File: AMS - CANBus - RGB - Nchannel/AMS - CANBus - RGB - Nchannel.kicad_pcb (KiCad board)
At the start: 2 copper layers, 72.9 x 71.1 mm, 59 parts, among them J1 Power_And_CAN, J2 Screw_Terminal_01x05, J3 TTL_Programmer, J4 ICSP, J5 Conn_01x02, Q1 IRF9Z34NPBF, Q10 2N7002, Q2 2N7002, Q3 IRF9Z34NPBF, Q4 2N7002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

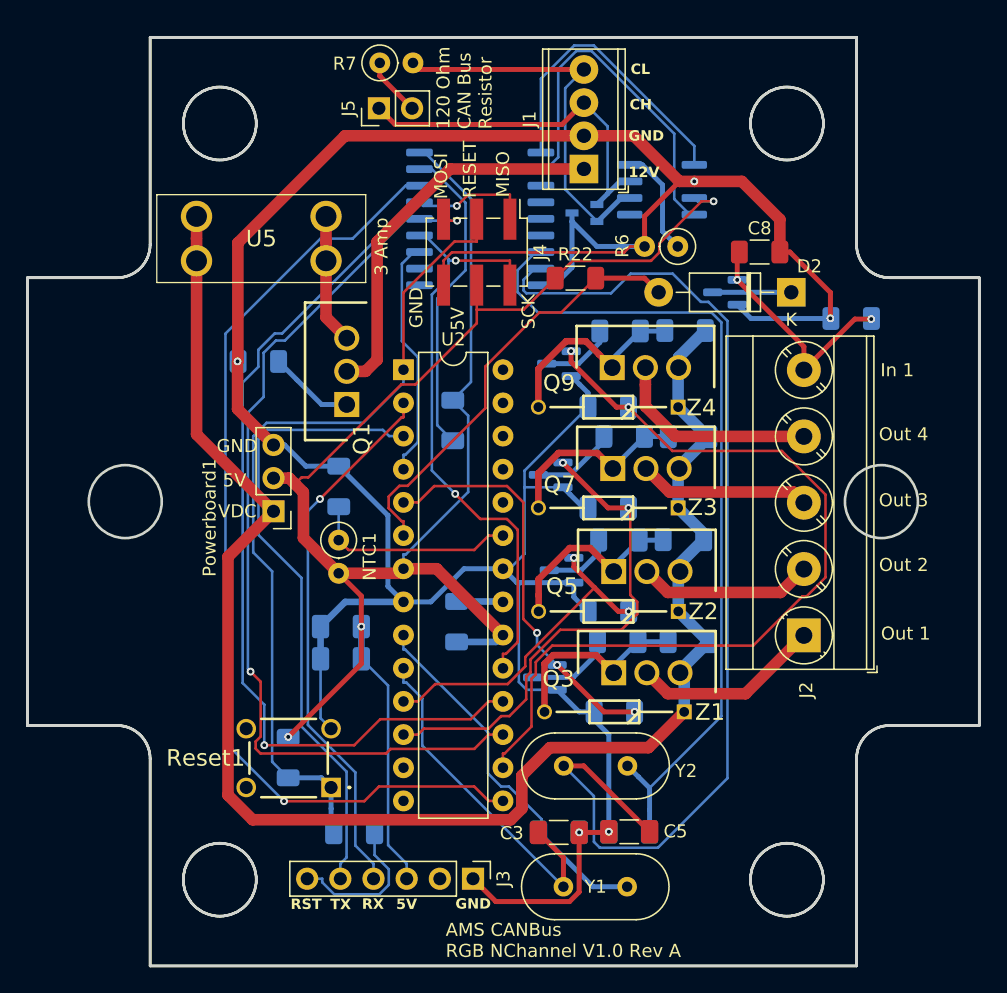
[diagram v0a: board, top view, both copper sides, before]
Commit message: clean up to avoid serpac case mounting bosses.
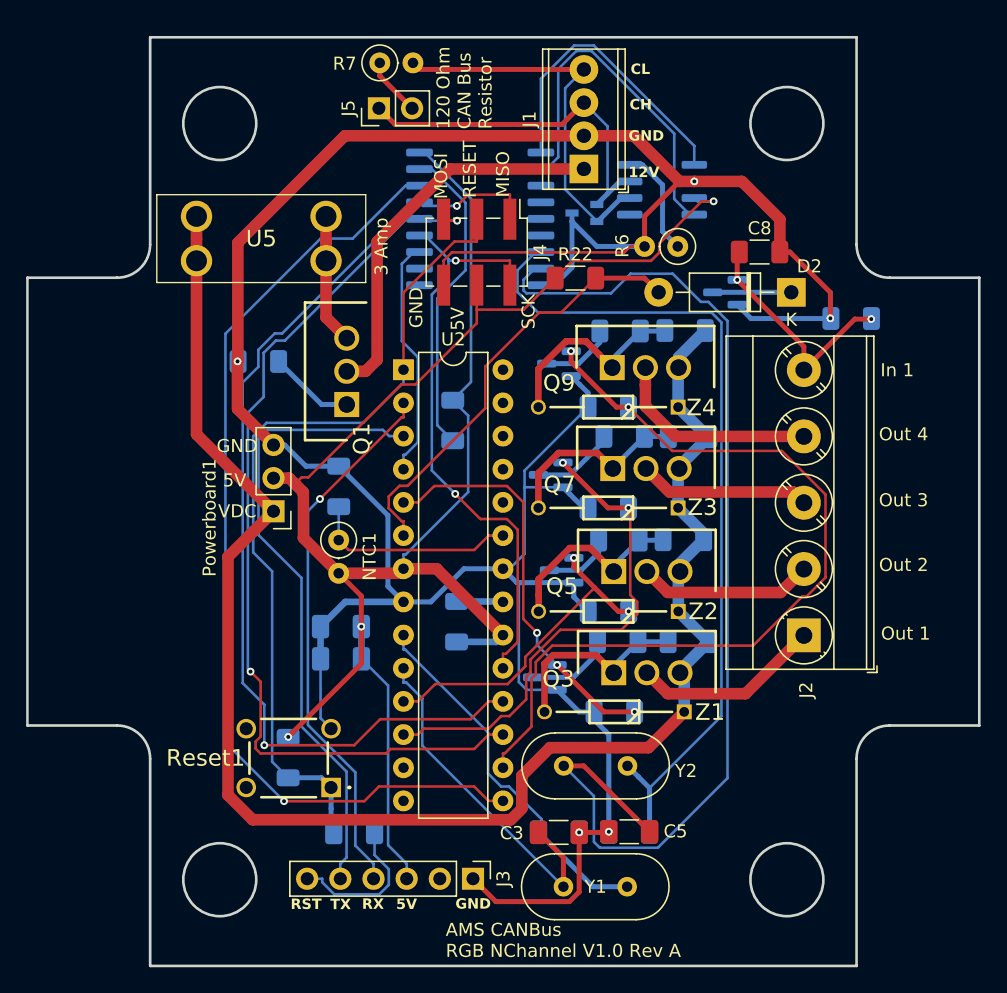
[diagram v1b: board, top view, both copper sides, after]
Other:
- outline, holes or cut-outs redrawn

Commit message: routing and stuff are fixed along with the addition of the I2c bus being pulled out.
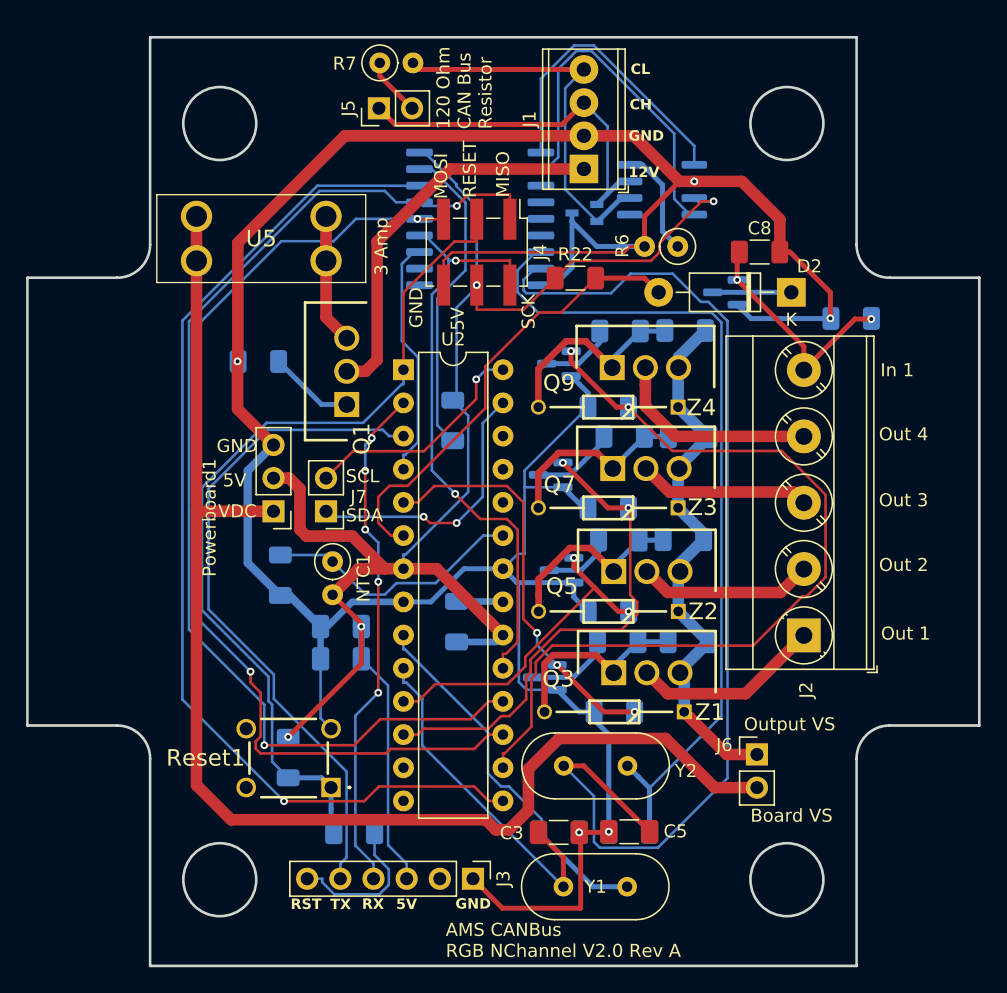
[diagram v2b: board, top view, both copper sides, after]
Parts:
- added J6: Conn_01x02, Connector_PinHeader_2.54mm:PinHeader_1x02_P2.54mm_Vertical, F.Cu at (168.0, 111.2)
- added J7: Conn_01x02, Connector_PinHeader_2.54mm:PinHeader_1x02_P2.54mm_Vertical, F.Cu at (135.0, 92.6)
- moved R3 8.14 mm to (131.5, 97.5), turned to 90 degrees
- moved NTC1 1.71 mm to (135.5, 96.5)
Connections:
- Q3 pad 3: +VDC -> /Output12v/VS
- Q5 pad 3: +VDC -> /Output12v/VS
- Q7 pad 3: +VDC -> /Output12v/VS
- Q9 pad 3: +VDC -> /Output12v/VS
- R12 pad 1: +VDC -> /Output12v/VS
- R15 pad 1: +VDC -> /Output12v/VS
- R18 pad 1: +VDC -> /Output12v/VS
- R9 pad 1: +VDC -> /Output12v/VS
- U2 pad 27: /BareMinAtmel328P/PC4-A4-SDA -> SDA
- U2 pad 28: /BareMinAtmel328P/PC5-A5-SCL -> SCL
- Z1 pad 1: +VDC -> /Output12v/VS
- Z2 pad 1: +VDC -> /Output12v/VS
- Z3 pad 1: +VDC -> /Output12v/VS
- Z4 pad 1: +VDC -> /Output12v/VS
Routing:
- net /Output12v/VS: track 0.00 -> 41.4 mm
- net +VDC: track 125.0 -> 100.1 mm
- net SDA: track 0.00 -> 20.4 mm, vias 0 -> 2
- net SCL: track 0.00 -> 17.9 mm, vias 0 -> 1
- net +5V: track 147.0 -> 129.8 mm, vias 3 -> 4
- net /BareMinAtmel328P/PB4-D12-MISO: track 77.0 -> 85.9 mm
- net /BareMinAtmel328P/PB3-D11-MOSI: track 70.9 -> 76.8 mm
- net /BareMinAtmel328P/PB1-D9: track 74.9 -> 80.2 mm
- net /BareMinAtmel328P/PC0-A0: track 15.9 -> 20.2 mm
- net /BareMinAtmel328P/RESET: track 64.8 -> 68.1 mm
- net /BareMinAtmel328P/PD1-TX: track 48.3 -> 51.5 mm
- net /BareMinAtmel328P/PD0-RX: track 41.6 -> 39.4 mm, vias 1 -> 5
- net /BareMinAtmel328P/PD4-D4: track 33.5 -> 35.1 mm
- net GND: track 233.9 -> 235.0 mm
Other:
- board text added: "AMS CANBus RGB NChannel V2.0 Rev A"
- board text added: "Board VS"
- board text added: "Output VS"
- board text added: "SCL"
- board text added: "SDA"
- board text removed: "AMS CANBus RGB NChannel V1.0 Rev A"
